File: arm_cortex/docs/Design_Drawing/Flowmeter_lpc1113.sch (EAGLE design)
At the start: 99 parts, among them IC1 LM7805, IC2 LM324N, IC5 OP07CN, Q4 BSS92, Q5 BSS295, U1 LPC1113FBD48/302,1, U2 LD1117S33CTR, U4 MAX232ACSE+, U5 MAX485CSA+, X1 MKDSN1,5/3-5,08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

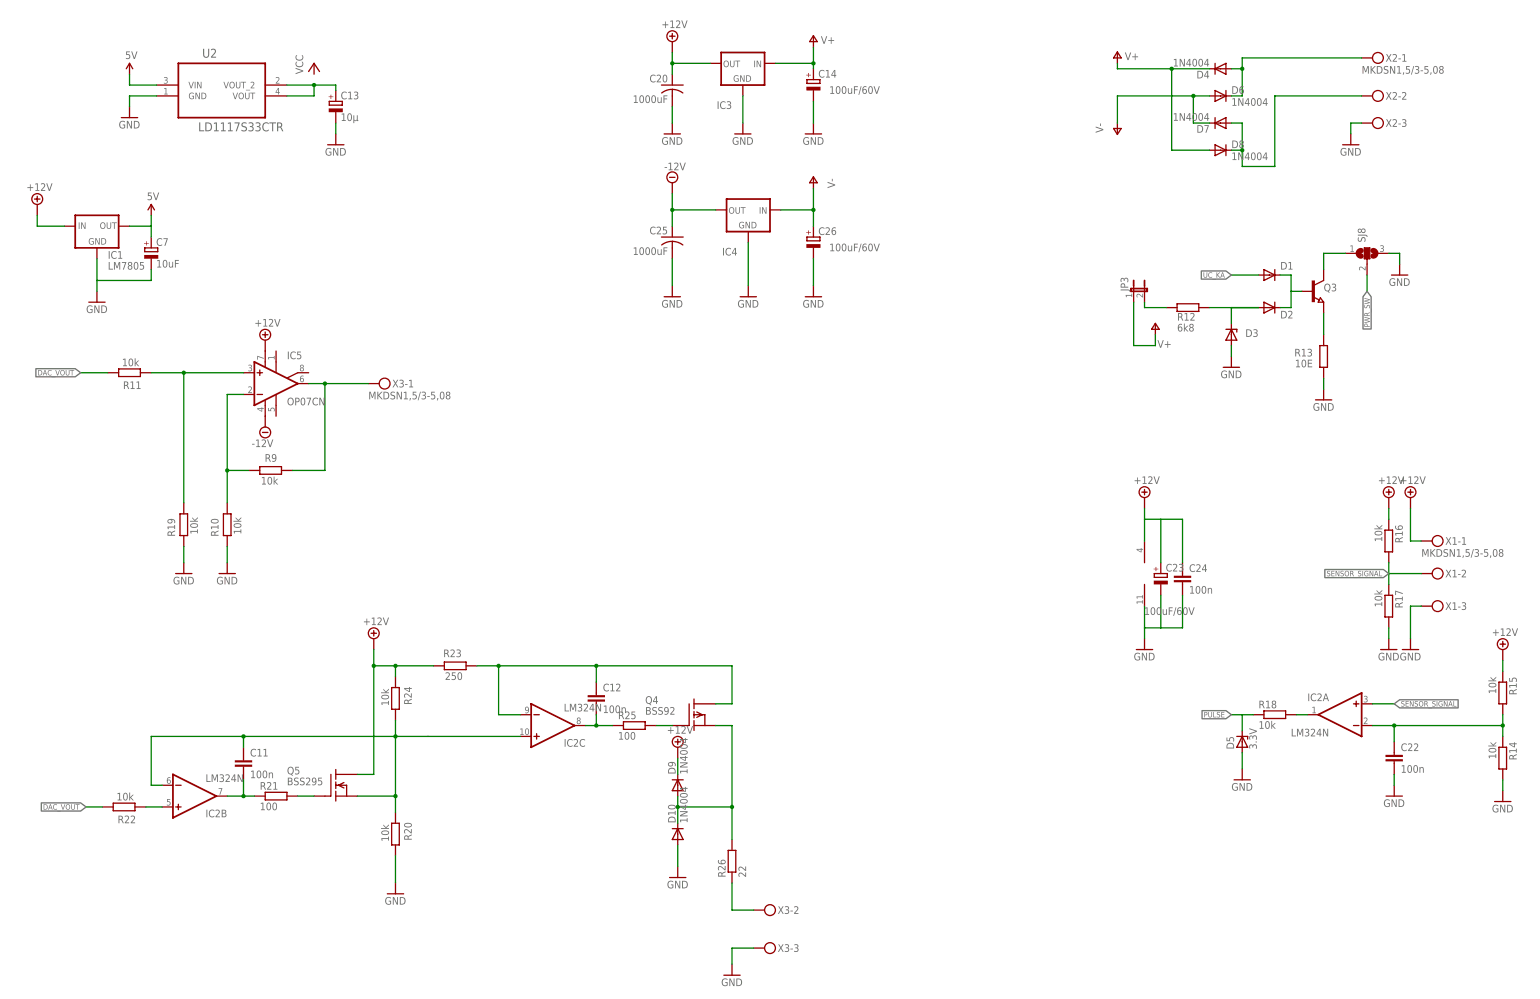
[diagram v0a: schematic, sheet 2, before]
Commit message: removed 4-20mA translation circuit. removed the power 10V supply. added +12V and -12V supply regulator. added bridge rectifier
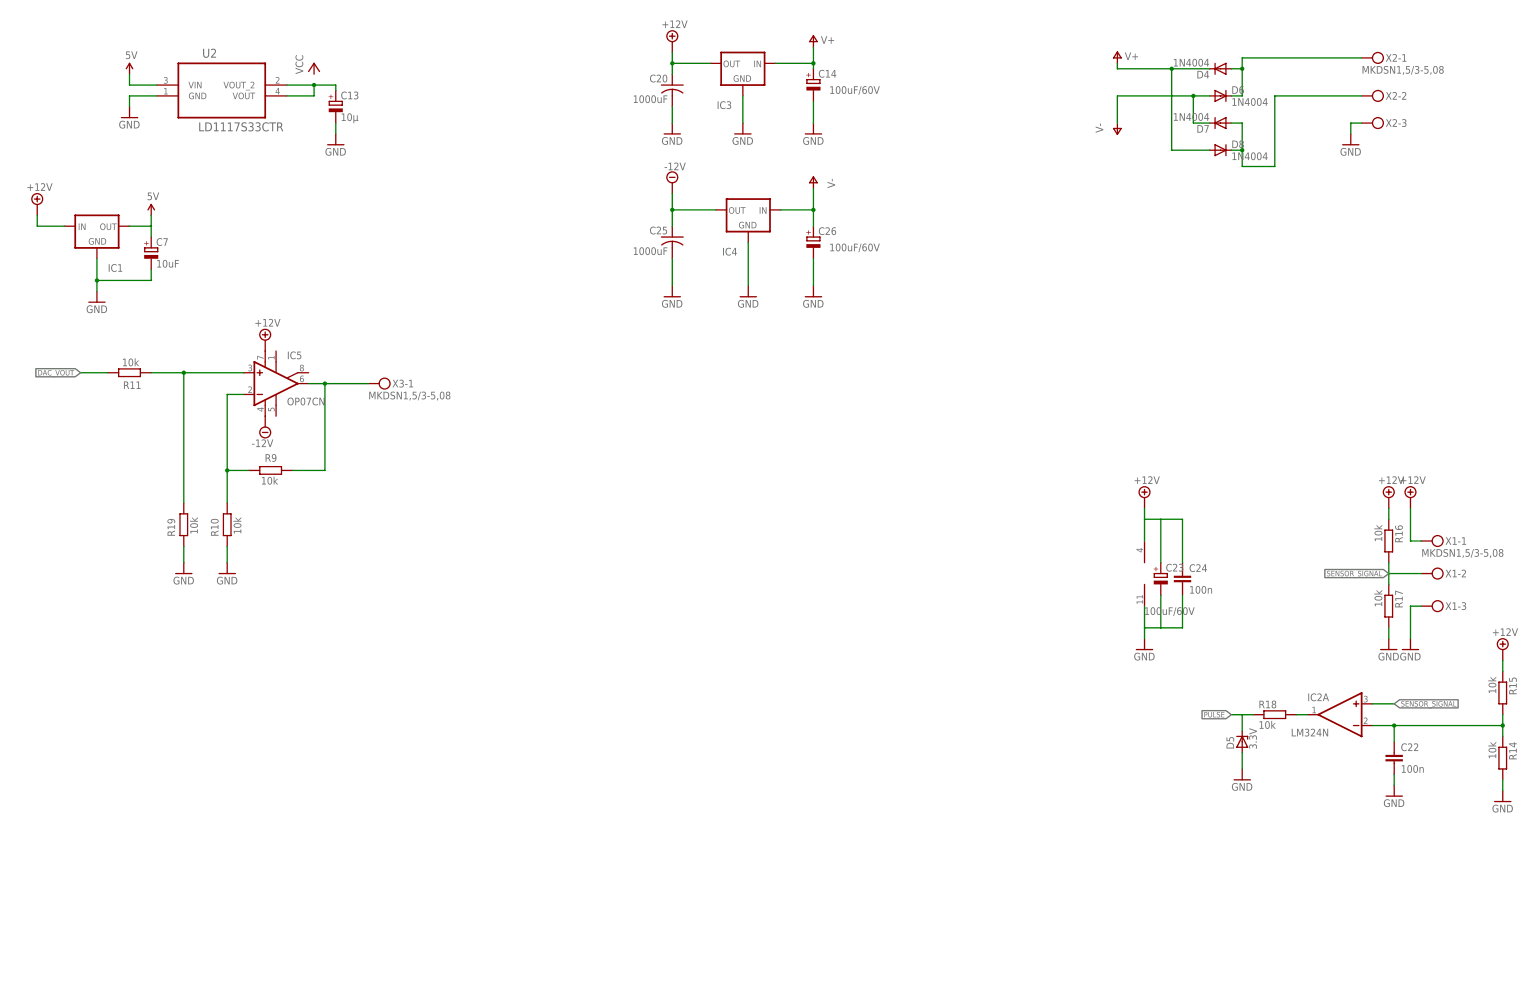
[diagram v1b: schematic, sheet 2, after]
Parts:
- removed C11, C12: 100n, rcl:C-EUC0805K
- removed D1, D2: (no value), diode:DIODE-MINIMELF
- removed D10, D9: 1N4004, diode:1N4004
- removed D3: (no value), fabisp:NG_ZENER_DIODESOD123
- removed JP3: (no value), jumper:JP1E
- removed PRG_SW1: (no value), SparkFun1:TAC_SWITCHSMD
- removed Q3: (no value), semicon-smd-ipc:NPN-TRANSISTOR_SOT23W
- removed Q4: BSS92, transistor-fet:BSS92
- removed Q5: BSS295, transistor-fet:BSS295
- removed R12: 6k8, rcl:R-EU_R0805
- removed R13: 10E, rcl:R-EU_R0805
- removed R20, R22, R24: 10k, resistor:R-EU_0207/10
- removed R21, R25: 100, rcl:R-EU_R0805W
- removed R23: 250, resistor:R-EU_0207/10
- removed R26: 22, rcl:R-EU_R0805W
- removed SJ8: (no value), jumper:SJ2W
- added RST_SW: (no value), SparkFun1:TAC_SWITCHSMD
- IC1: value LM7805 -> (none); device SparkFun5:V_REG_78XXSIDE -> v-reg:79XXS
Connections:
- removed net N$19: D1.C, D2.C, Q3.B
- removed net N$20: C11.2, IC2B.OUT, R21.1
- removed net N$21: Q3.E, R13.2
- removed net N$22: D2.A, D3.CATHODE, R12.2
- removed net N$23: JP3.2, R12.1
- removed net N$25: Q3.C, SJ8.1
- removed net N$40: Q5.G, R21.2
- removed net N$44: C12.1, IC2C.-IN, Q4.D, R23.2
- removed net N$45: C11.1, IC2B.-IN, IC2C.+IN, Q5.S, R20.1, R24.2
- removed net N$46: IC2B.+IN, R22.1
- removed net N$47: C12.2, IC2C.OUT, R25.1
- removed net N$48: Q4.G, R25.2
- removed net N$50: R26.1, X3-2.KL
- removed net N$51: D10.C, D9.A, Q4.S, R26.2
- removed net PWR_SW: SJ8.2
- removed net UC_KA: D1.A, U1B.PIO0_8/MISO0/CT16B0_MAT0
- net +12V: no longer D9.C, Q5.D, R23.1, R24.1
- net DAC_VOUT: no longer R22.2
- net GND: now also RST_SW.2; no longer D10.A, D3.ANODE, PRG_SW1.2, R13.1, R20.2, SJ8.3, X3-3.KL
- net N$4: now also RST_SW.4; no longer PRG_SW.4
- net N$5: now also PRG_SW.4; no longer PRG_SW1.4
- net V+: no longer JP3.1
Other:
- moved on the sheet: PRG_SW

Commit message: removed +12V -12V regulators. added connector for input regulated 12V added lm321 inplace of lm324
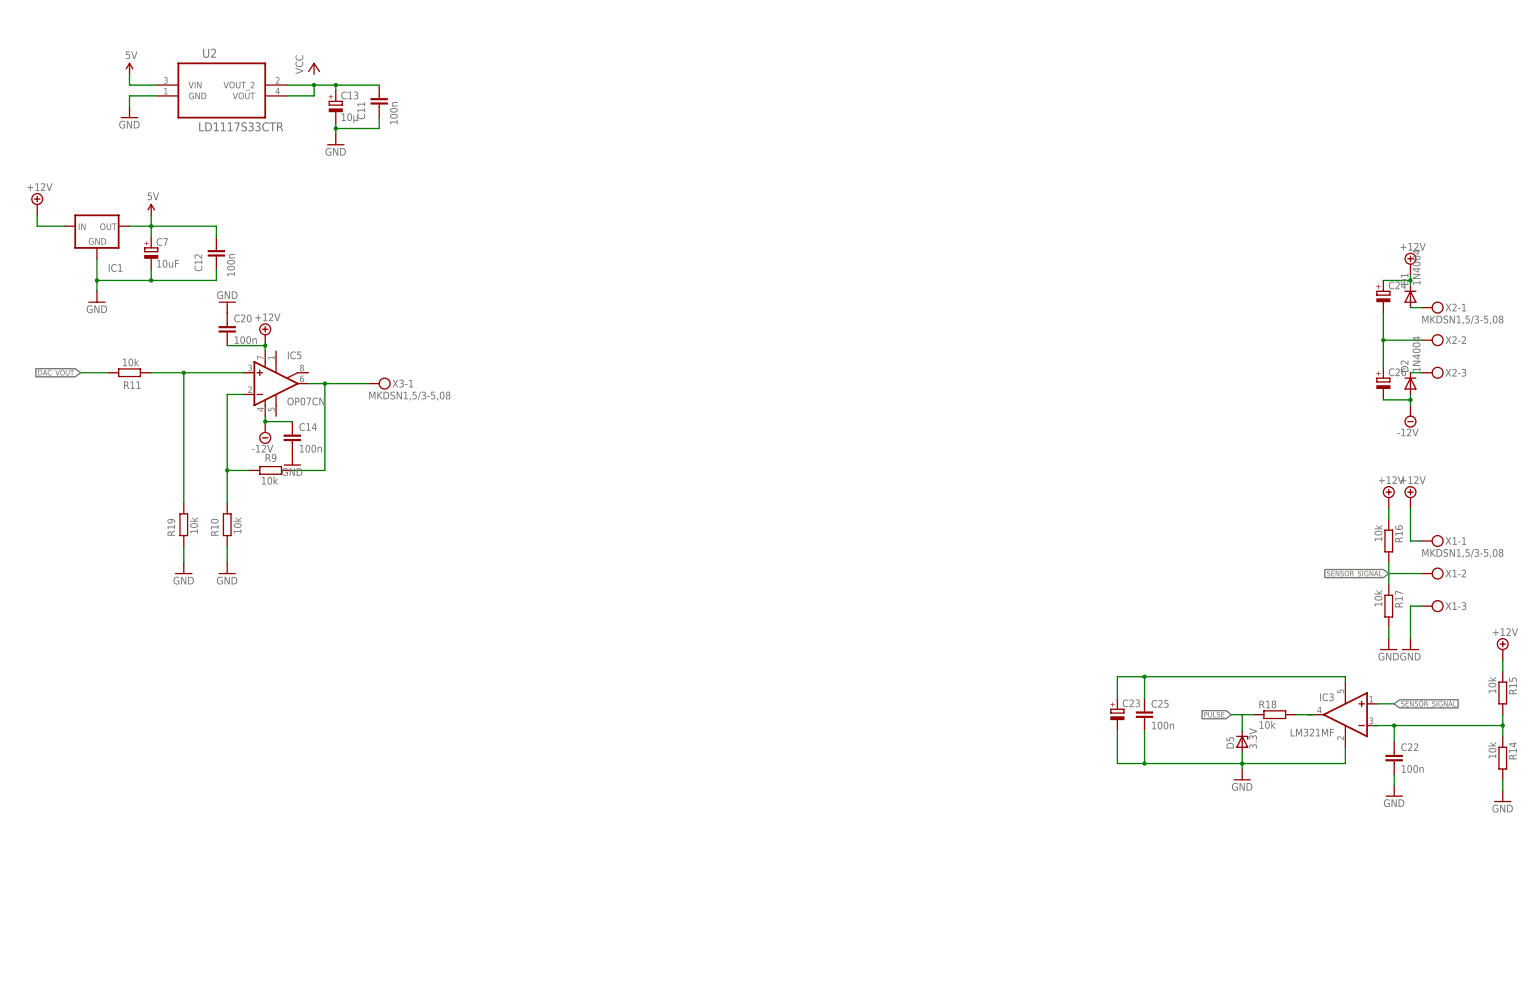
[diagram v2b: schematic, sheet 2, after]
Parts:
- removed D4, D6, D7, D8: 1N4004, diode:1N4004
- removed IC2: LM324N, linear:LM324N
- removed IC4: (no value), v-reg:79XXS
- added C11, C12: 100n, rcl:C-EUC0805K
- added D1, D2: 1N4004, diode:1N4004
- C14: value 100uF/60V -> 100n; device rcl:CPOL-EUE5-6 -> rcl:C-EUC0805K
- C20, C25: value 1000uF -> 100n; device rcl:C-US050-035X075 -> rcl:C-EUC0805K
- C24: value 100n -> 100uF/60V; device rcl:C-EUC0805K -> rcl:CPOL-EUE5-6
- IC3: value (none) -> LM321MF; device v-reg:79XXS -> linear:LM321MF
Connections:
- removed net N$32: IC3.OUT
- removed net N$38: D7.A, D8.C, X2-2.KL
- removed net N$39: D4.A, D6.C, X2-1.KL
- removed net V+: C14.+, D4.C, D8.A, IC3.IN
- removed net V-: C26.+, D6.A, D7.C, IC4.IN
- new net N$19: C24.-, C26.+, X2-2.KL
- new net N$20: D2.C, X2-3.KL
- new net N$21: D1.A, X2-1.KL
- new net N$22: C23.+, C25.1, IC3.V+
- net +12V: now also C20.2, C24.+, D1.C; no longer C20.1, C23.+, C24.1, IC2P.V+
- net -12V: now also C14.1, C26.-, D2.A; no longer C25.1, IC4.OUT
- net 5V: now also C12.2
- net GND: now also C11.1, C12.1, C14.2, C20.1, IC3.V-; no longer C14.-, C20.2, C24.2, C26.-, IC2P.V-, IC3.GND, IC4.GND, X2-3.KL
- net N$15: now also IC3.-IN; no longer IC2A.-IN
- net N$37: now also IC3.OUT; no longer IC2A.OUT
- net N$43: now also C11.2
- net SENSOR_SIGNAL: now also IC3.+IN; no longer IC2A.+IN
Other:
- moved on the sheet: C20, C23, C25, C26, X2-1, X2-2, X2-3

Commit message: removed led mosfets
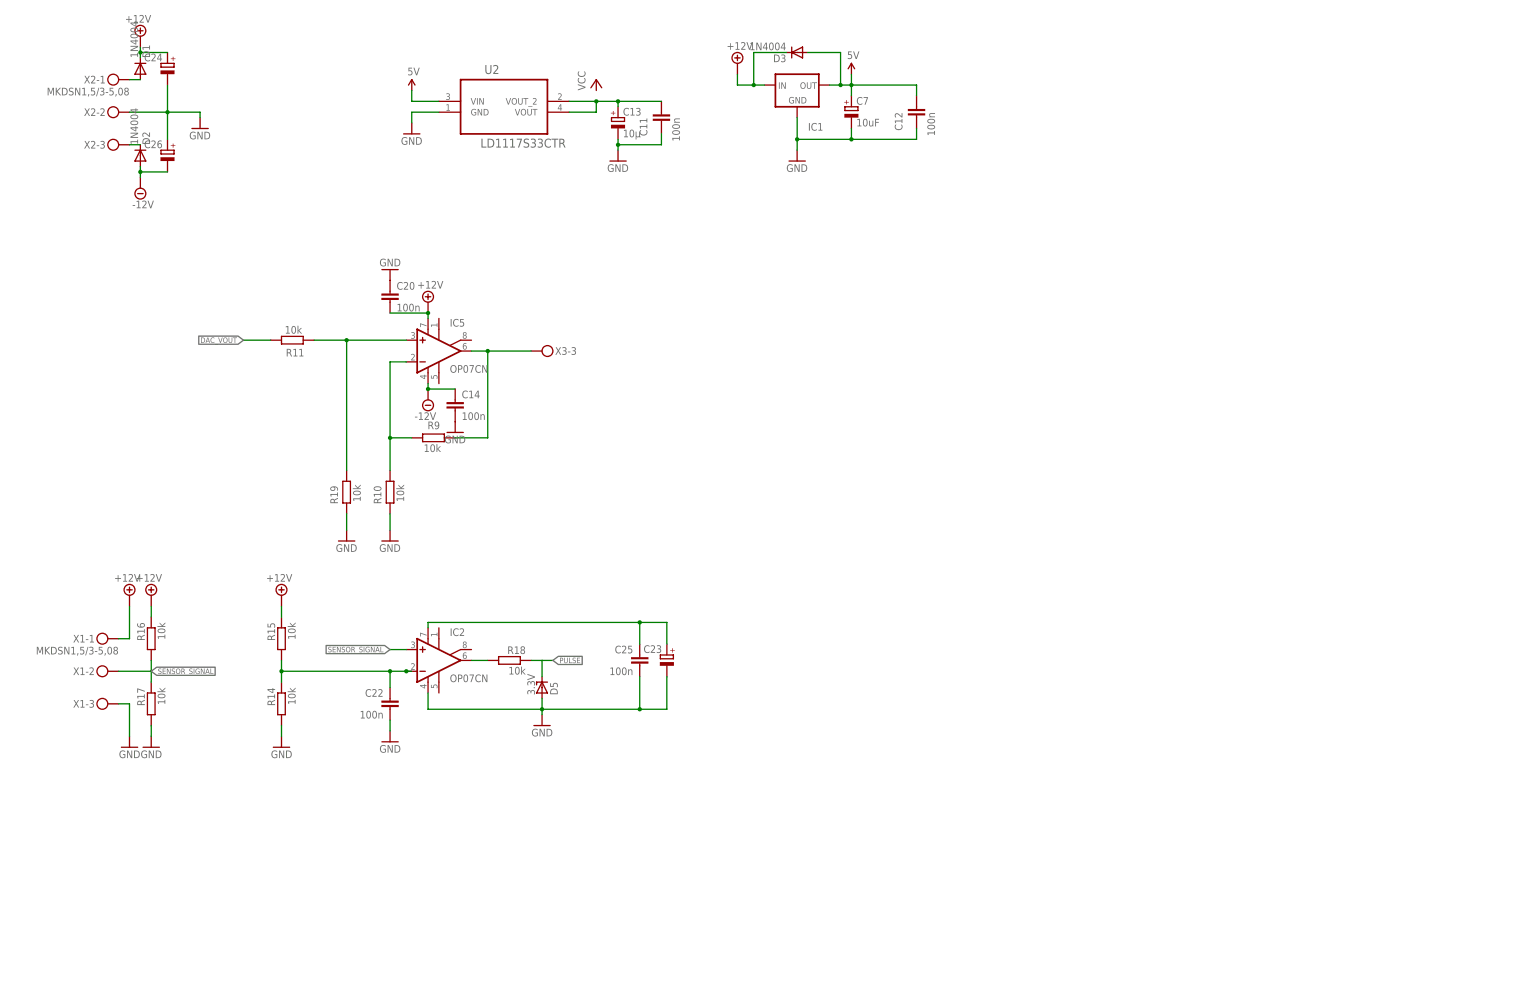
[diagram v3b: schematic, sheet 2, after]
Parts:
- removed IC3: LM321MF, linear:LM321MF
- removed JP4: (no value), jumper:JP2E
- removed JP5: (no value), jumper:JP1E
- removed Q1, Q2: (no value), semicon-smd-ipc:NPN-TRANSISTOR_SOT23W
- removed SJ6, SJ7: (no value), jumper:SJ
- removed SV1: (no value), con-amp-mt6:MT6-3
- added D3: 1N4004, diode:1N4004
- added IC2: OP07CN, linear:OP07CN
- added X4: MKDSN1,5/3-5,08, con-phoenix-508:MKDSN1,5/3-5,08
- C22: device rcl:C-EUC0805K -> rcl:C-EU025-024X044
- D5: device ng:ZENER_DIODESOD123 -> ng:ZENER_DIODEDO41Z10
- R14, R15, R16, R17, R18: device rcl:R-EU_R0805W -> rcl:R-EU_0207/10
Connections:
- removed net N$11: SJ7.1, SV1-3.S
- removed net N$12: SJ6.1, SV1-1.S
- removed net N$19: C24.-, C26.+, X2-2.KL
- removed net N$3: Q2.B, R5.1
- removed net N$35: Q1.B, R4.1
- removed net RXD: SJ6.2
- removed net TXD: SJ7.2
- net +12V: now also D3.C
- net 5V: now also D3.A
- net GND: now also C24.-, C26.+, IC2.V-, X2-2.KL, X4-2.KL; no longer IC3.V-, JP4.3, Q1.E, Q2.E, SV1-2.S
- net LED1: now also U1A.PIO3_5_
- net LED2: now also U1A.PIO2_5_
- net N$1: now also R4.1; no longer Q1.C
- net N$15: now also IC2.-IN; no longer IC3.-IN
- net N$2: now also R5.1; no longer Q2.C
- net N$22: now also IC2.V+; no longer IC3.V+
- net N$30: now also X4-1.KL; no longer JP4.1
- net N$31: now also X4-3.KL; no longer JP4.2
- net N$33: now also X3-3.KL; no longer X3-1.KL
- net N$34: now also X3-1.KL; no longer JP5.1
- net N$36: now also X3-2.KL; no longer JP5.2
- net N$37: now also IC2.OUT; no longer IC3.OUT
- net SENSOR_SIGNAL: now also IC2.+IN; no longer IC3.+IN
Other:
- moved on the sheet: C11, C12, C13, C14, C20, C22, C23, C24, C25, C26, C7, D1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

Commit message: 
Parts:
- removed IC1: (no value), v-reg:79XXS
- removed SJ1, SJ2, SJ3, SJ4, SJ5: (no value), jumper:SJ
- removed U$1: MCP4921-E/P, microchip:MCP4921-E/P
- added C27, C28: 100n, rcl:C-EUC0805K
- added JP3: (no value), pinhead:PINHD-1X6
- added L1, L2: WURTH ELEKTRONIK - 742792095, wuerth-elektronik:WE-CBF_0805
- added R12, R13, R20, R21, R22, R23: 10k, rcl:R-EU_R0805W
- added U6: 7805TV, linear:7805TV
- added U7: MCP4921-E/P, microchip:MCP4921-E/P
- added U8: SP1490, exar:SP1490
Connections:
- removed net N$10: JP2.1, SJ5.1
- removed net N$18: U$1.AVSS
- removed net N$30: U4.R1OUT, X4-1.KL
- removed net N$31: U4.T1OUT, X4-3.KL
- removed net N$34: U5.A, X3-1.KL
- removed net N$36: U5.B, X3-2.KL
- removed net N$6: JP2.5, SJ1.1
- removed net N$7: JP2.2, SJ4.2
- removed net N$8: JP2.4, SJ3.2
- removed net N$9: JP2.6, SJ2.2
- new net A: U5.A, U8.A, U8.Y, X3-2.KL
- new net B: U5.B, U8.B, U8.Z, X3-1.KL
- new net GND1: C10.2, C27.2, C9.-, L1.2, U7.AVSS
- new net N$11: C10.1, C27.1, C9.+, L2.1, U7.VDD, U7.VREFA
- new net N$12: U4.T1OUT, X4-2.KL
- new net SWITCH0: JP3.1, R23.2
- new net SWITCH1: JP3.2, R22.2
- new net SWITCH2: JP3.3, R21.2
- new net SWITCH3: JP3.4, R20.2
- new net SWITCH4: JP3.5, R13.2
- new net SWITCH5: JP3.6, R12.2
- new net UART_RX1: U8.RO
- net +12V: now also U6.VI; no longer IC1.IN
- net /RESET: now also JP2.5; no longer SJ1.2
- net 5V: now also C16.-, C19.2, C21.2, C28.2, L2.2, U4.VCC, U5.VCC, U6.VO, U8.VCC; no longer IC1.OUT
- net DAC_VOUT: now also U7.VOUTA; no longer U$1.VOUTA
- net GND: now also C28.1, JP2.1, L1.1, U4.GND, U6.GND, U8.GND, X4-1.KL; no longer C10.2, C9.-, IC1.GND, SJ5.2, X4-2.KL
- net LCD_EN: now also U1B.PIO3_2/!DCD!; no longer U1A.PIO1_8/CT16B1_CAP0
- net LCD_R/W: now also U1B.PIO3_1/!DSR!; no longer U1A.PIO1_9/CT16B1_MAT0_
- net LCD_RS: now also U1B.PIO3_0/!DTR!; no longer U1B.PIO1_10/AD6/CT16B1_MAT1
- net LDAC: now also U1B.PIO3_3/!RI!, U7.~LDAC; no longer U$1.~LDAC, U1B.PIO3_1/!DSR!
- net N$13: now also U4.R1OUT, X4-3.KL; no longer U$1.VREFA
- net SPI1_CS: now also U7.~CS; no longer U$1.~CS
- net SPI1_MOSI: now also U7.SDI; no longer U$1.SDI
- net SPI1_SCK: now also U7.SCK; no longer U$1.SCK
- net SWDCLK: now also JP2.6; no longer SJ2.1
- net SWDIO: now also JP2.4; no longer SJ3.1
- net UART_TX: now also U8.DI
- net VCC: now also JP2.2, R12.1, R13.1, R20.1, R21.1, R22.1, R23.1; no longer C10.1, C16.-, C19.2, C21.2, C9.+, SJ4.1, U$1.VDD, U4.VCC, U5.VCC
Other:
- moved on the sheet: C10, C12, C15, C16, C17, C18, C19, C21, C5, C7, C9, D3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
